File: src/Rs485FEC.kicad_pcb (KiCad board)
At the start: 2 copper layers, 24 x 27.9 mm, 19 parts, among them J1 B3B-XH-A, P1 105444-0001, Q1 DMP3099L-13, U1 FT232RL, U2 SP485E

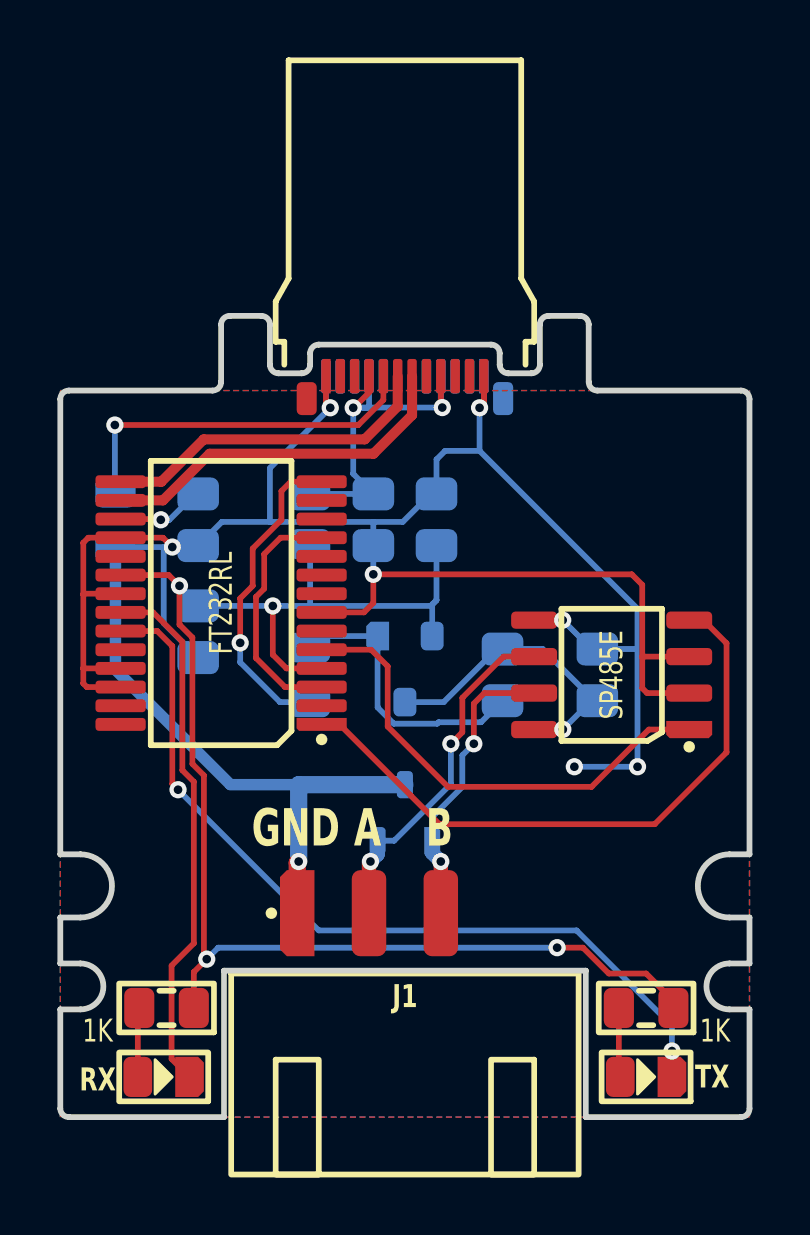
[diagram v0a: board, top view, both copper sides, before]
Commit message: Fixed TXDEN signal
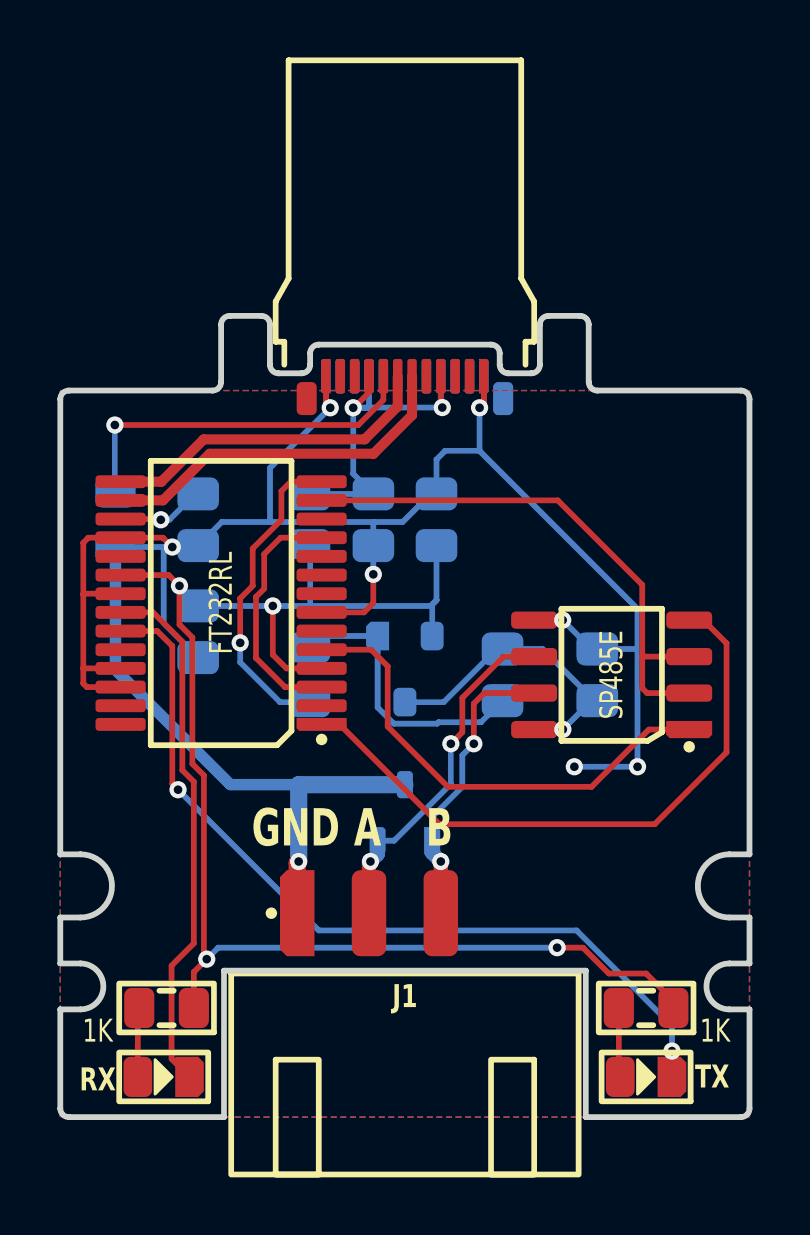
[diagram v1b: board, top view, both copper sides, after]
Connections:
- U2 pad 2: GND -> TXDEN
- U2 pad 3: GND -> TXDEN
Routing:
- net TXDEN: track 0.00 -> 19.3 mm
- net GND: track 105.1 -> 88.6 mm
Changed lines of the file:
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@@
       (net 4 "RXD") (thermal_bridge_angle 45))
     (pad "2" smd roundrect (at -2.7 -0.635 180) (size 1.6 0.6) (layers "F.Cu" "F.Paste" "F.Mask") (roundrect_rratio 0.25)
-      (net 7 "GND") (thermal_bridge_angle 45))
+      (net 19 "TXDEN") (thermal_bridge_angle 45))
     (pad "3" smd roundrect (at -2.7 0.635 180) (size 1.6 0.6) (layers "F.Cu" "F.Paste" "F.Mask") (roundrect_rratio 0.25)
-      (net 7 "GND") (thermal_bridge_angle 45))
+      (net 19 "TXDEN") (thermal_bridge_angle 45))
     (pad "4" smd roundrect (at -2.7 1.905 180) (size 1.6 0.6) (layers "F.Cu" "F.Paste" "F.Mask") (roundrect_rratio 0.25)
       (net 2 "TXD") (thermal_bridge_angle 45))
@@
   (segment (start 23.575 26.425) (end 22.1 26.425) (width 0.35) (layer "F.Cu") (net 6))
   (segment (start 29.1 30.325) (end 30.575 30.325) (width 0.2) (layer "F.Cu") (net 7))
-  (segment (start 40.265 31.865) (end 40.265 29.365) (width 0.2) (layer "F.Cu") (net 7))
-  (segment (start 39.9 29) (end 30.9 29) (width 0.2) (layer "F.Cu") (net 7))
   (segment (start 34.75 22.1) (end 34.75 23.05) (width 0.2) (layer "F.Cu") (net 7))
-  (segment (start 41.9 33.135) (end 40.435 33.135) (width 0.2) (layer "F.Cu") (net 7))
   (segment (start 23.575 27.725) (end 23.9 28.05) (width 0.2) (layer "F.Cu") (net 7))
   (segment (start 20.8 29.7) (end 20.825 29.675) (width 0.2) (layer "F.Cu") (net 7))
@@
   (segment (start 20.8 27.9) (end 20.975 27.725) (width 0.2) (layer "F.Cu") (net 7))
   (segment (start 30.575 30.325) (end 30.9 30) (width 0.2) (layer "F.Cu") (net 7))
-  (segment (start 40.265 29.365) (end 39.9 29) (width 0.2) (layer "F.Cu") (net 7))
   (segment (start 22.1 32.925) (end 20.925 32.925) (width 0.2) (layer "F.Cu") (net 7))
   (segment (start 28.25 40.8) (end 28.25 39.05) (width 0.6) (layer "F.Cu") (net 7))
@@
   (segment (start 20.975 27.725) (end 22.1 27.725) (width 0.2) (layer "F.Cu") (net 7))
   (segment (start 36.5 30.595) (end 37.495 30.595) (width 0.2) (layer "F.Cu") (net 7))
-  (segment (start 40.265 32.965) (end 40.265 31.865) (width 0.2) (layer "F.Cu") (net 7))
   (segment (start 20.825 29.675) (end 22.1 29.675) (width 0.2) (layer "F.Cu") (net 7))
-  (segment (start 41.9 31.865) (end 40.265 31.865) (width 0.2) (layer "F.Cu") (net 7))
   (segment (start 20.8 29.7) (end 20.8 27.9) (width 0.2) (layer "F.Cu") (net 7))
   (segment (start 28.25 39.05) (end 28.3 39) (width 0.6) (layer "F.Cu") (net 7))
@@
   (segment (start 34.50697 23.2) (end 34.75 22.95697) (width 0.2) (layer "F.Cu") (net 7))
   (segment (start 20.8 32.275) (end 20.8 29.7) (width 0.2) (layer "F.Cu") (net 7))
-  (segment (start 40.435 33.135) (end 40.265 32.965) (width 0.2) (layer "F.Cu") (net 7))
   (segment (start 20.8 32.8) (end 20.8 32.275) (width 0.2) (layer "F.Cu") (net 7))
   (segment (start 20.925 32.925) (end 20.8 32.8) (width 0.2) (layer "F.Cu") (net 7))
@@
   (segment (start 32.95 38.275) (end 32.95 37.45) (width 0.2) (layer "B.Cu") (net 18))
   (segment (start 34 36.4) (end 34 35.300006) (width 0.2) (layer "B.Cu") (net 18))
+  (segment (start 40.265 29.365) (end 40.265 31.865) (width 0.2) (layer "F.Cu") (net 19))
+  (segment (start 41.9 33.135) (end 40.435 33.135) (width 0.2) (layer "F.Cu") (net 19))
+  (segment (start 37.325 26.425) (end 40.265 29.365) (width 0.2) (layer "F.Cu") (net 19))
+  (segment (start 40.265 32.965) (end 40.265 31.865) (width 0.2) (layer "F.Cu") (net 19))
+  (segment (start 41.9 31.865) (end 40.265 31.865) (width 0.2) (layer "F.Cu") (net 19))
+  (segment (start 29.1 26.425) (end 37.325 26.425) (width 0.2) (layer "F.Cu") (net 19))
+  (segment (start 40.435 33.135) (end 40.265 32.965) (width 0.2) (layer "F.Cu") (net 19))
   (segment (start 27.825 32.925) (end 26.813909 31.913909) (width 0.2) (layer "F.Cu") (net 20))
   (segment (start 26.813909 29.786091) (end 27.1 29.5) (width 0.2) (layer "F.Cu") (net 20))

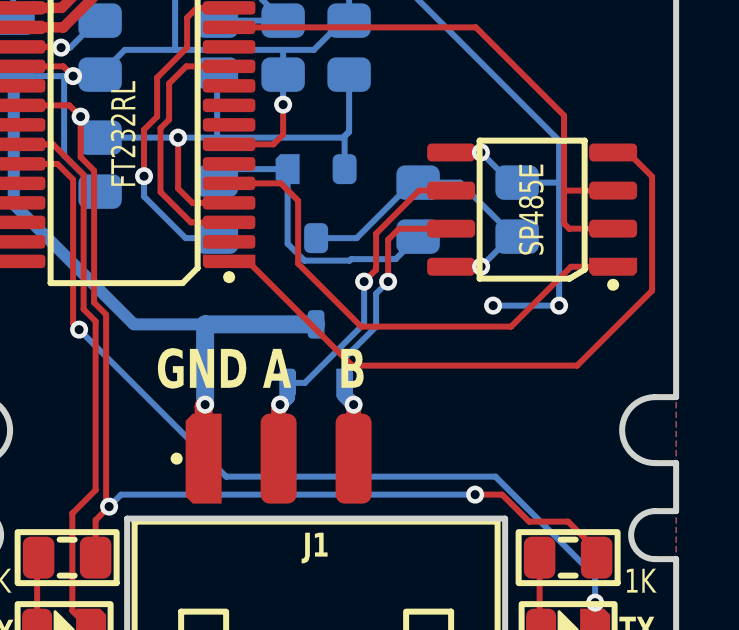
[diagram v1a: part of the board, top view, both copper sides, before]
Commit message: Added back fail-safe biased termination
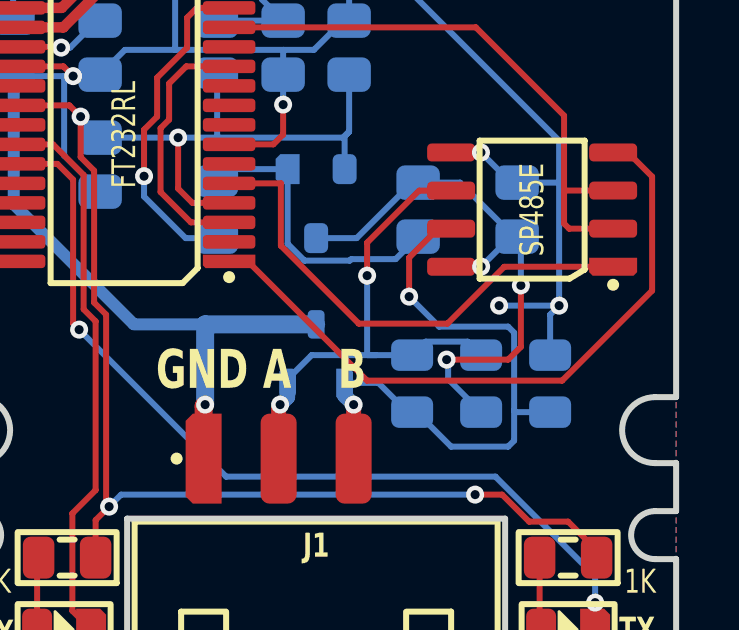
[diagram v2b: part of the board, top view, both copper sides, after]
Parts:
- added R1: 130, Medo64:R (0805), B.Cu at (35.2, 38.3)
- added R2: 750, Medo64:R (0805), B.Cu at (37.5, 38.3)
- added R3: 750, Medo64:R (0805), B.Cu at (39.8, 38.3)
- J1: value B3B-XH-A -> B4B-XH-A
- renumbered R1 to R4, R2 to R5, R3 to R6, R4 to R7
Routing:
- net B: track 10.2 -> 20.4 mm
- net 5V_SW: track 10.3 -> 18.8 mm, vias 1 -> 3
- net A: track 12.3 -> 17.4 mm
- net GND: track 88.6 -> 90.2 mm

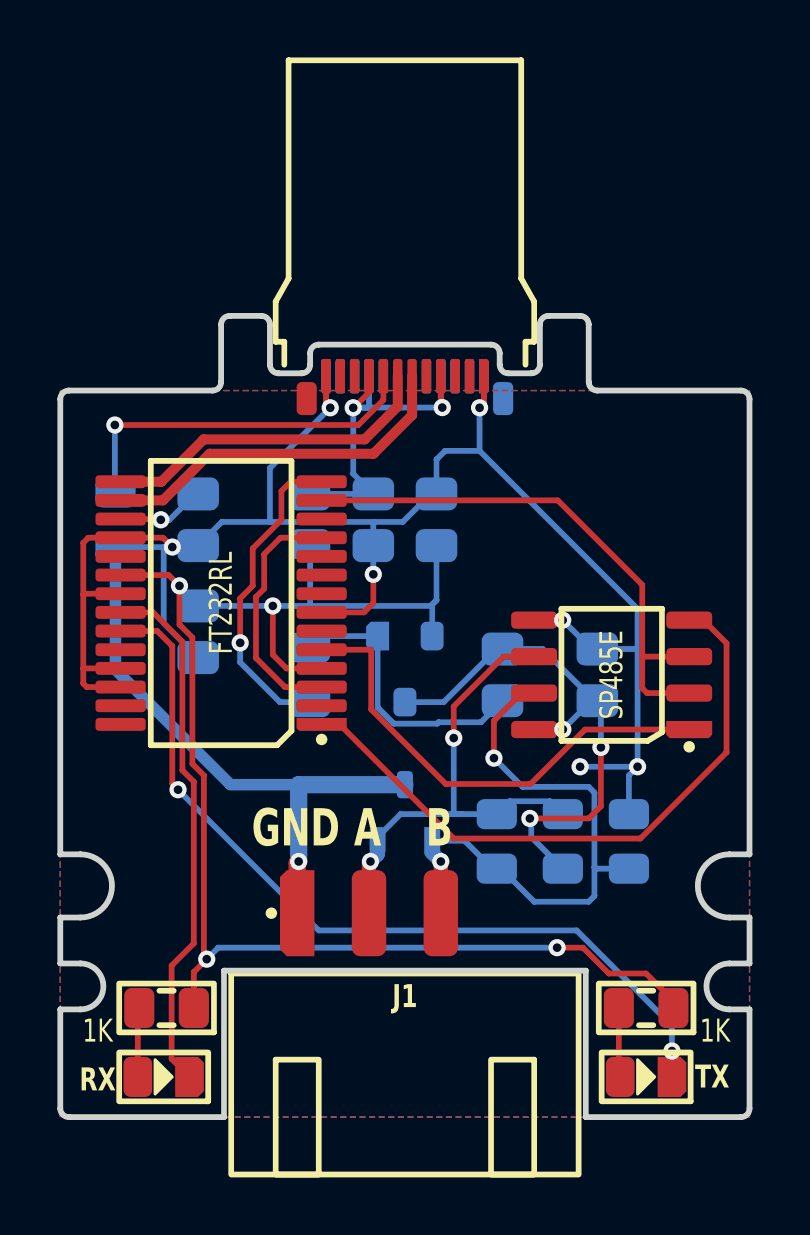
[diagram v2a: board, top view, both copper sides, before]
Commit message: Removed fail-safe termination
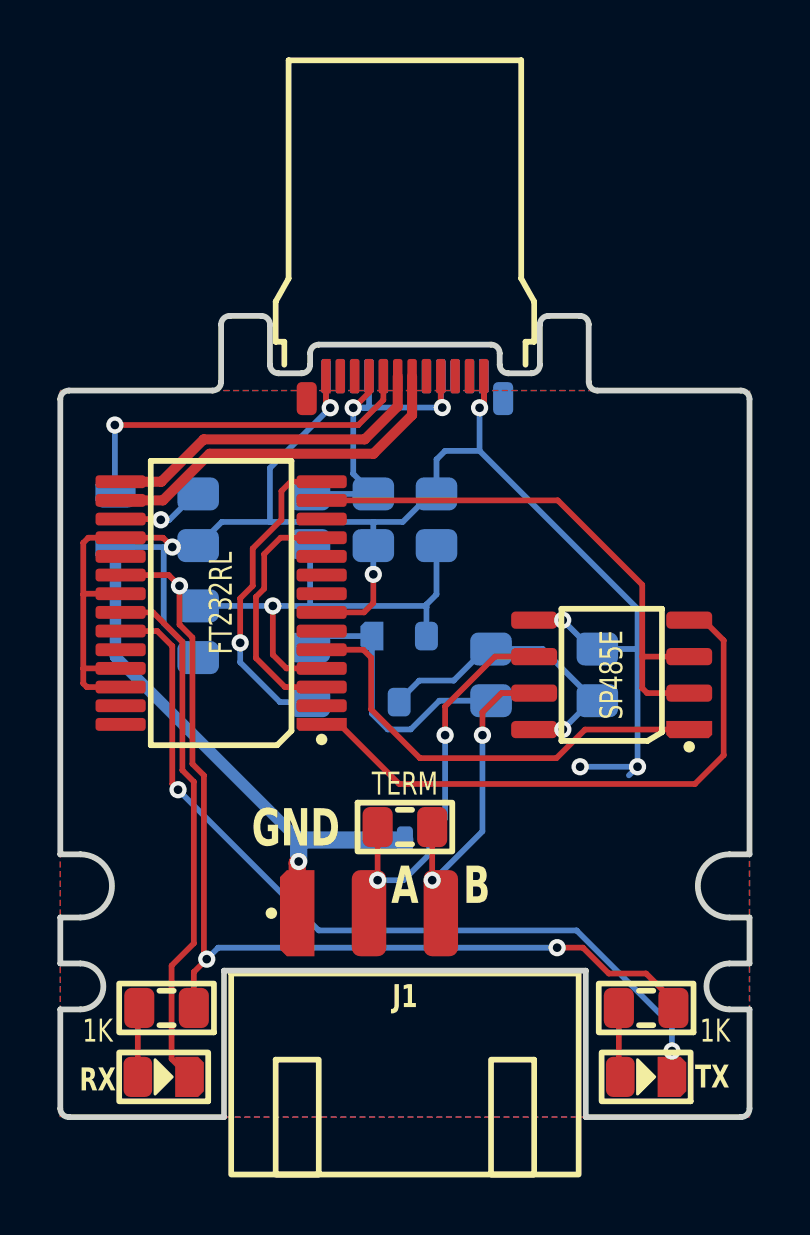
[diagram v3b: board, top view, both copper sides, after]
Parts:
- removed R2, R3: 750, Medo64:R (0805)
- R1: value 130 -> TERM; moved to F.Cu
- moved R1 3.24 mm to (32.0, 37.8), turned to 0 degrees
- moved D1 1.93 mm to (32.0, 39.2)
- moved C5 0.40 mm to (35.0, 32.5)
- moved Q1 0.20 mm to (31.8, 32.3)
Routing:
- net B: track 20.4 -> 11.1 mm
- net 5V_SW: track 18.8 -> 10.2 mm, vias 3 -> 1
- net A: track 17.4 -> 14.3 mm
- net GND: track 90.2 -> 87.5 mm
- net TXD: track 21.3 -> 19.6 mm
- net RXD: track 16.7 -> 15.8 mm

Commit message: Moving LEDs to bottom
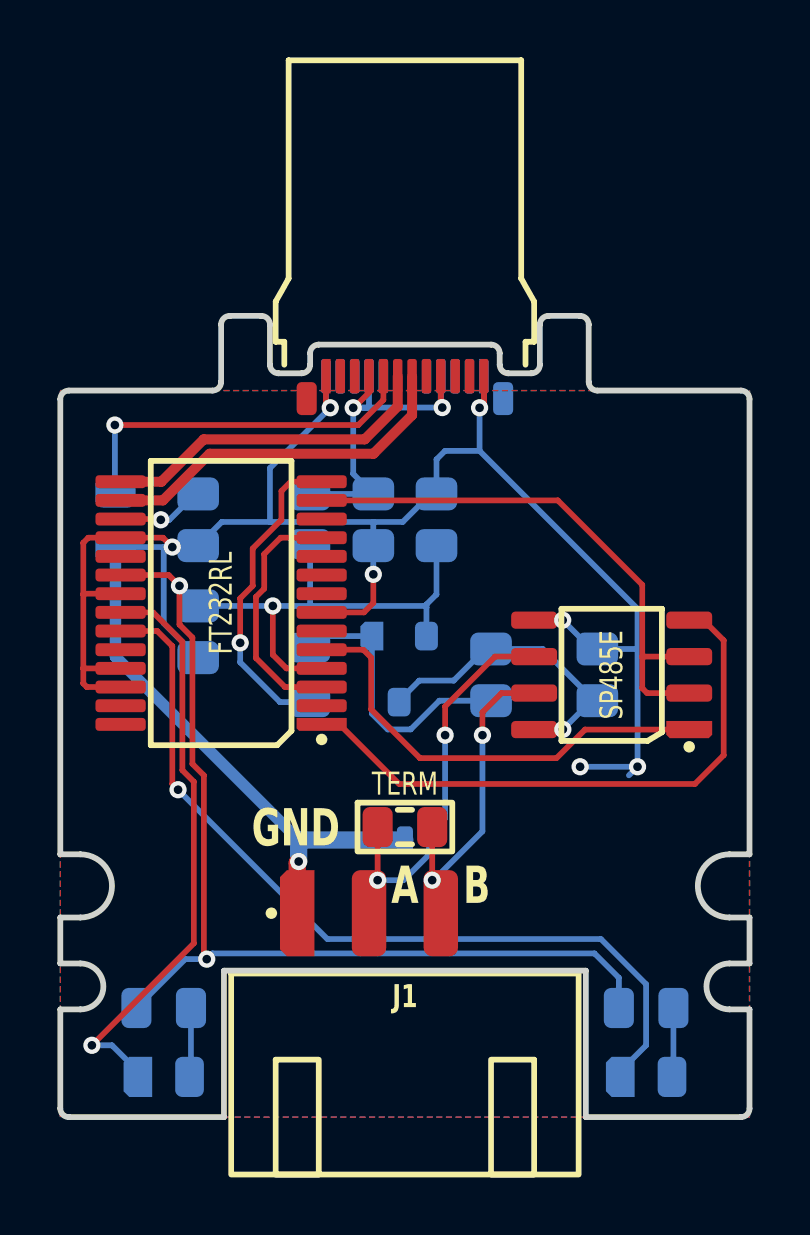
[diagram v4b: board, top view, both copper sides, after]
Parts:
- DS1, DS2, R4, R5: moved to B.Cu
- moved R4 0.10 mm to (23.6, 44.1), turned to 0 degrees
- turned DS1 to 0 degrees
- turned DS2 to 0 degrees
- turned R5 to 0 degrees
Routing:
- net LED_RXD: track 18.5 -> 20.2 mm, vias 0 -> 1
- net LED_TXD: track 29.5 -> 29.6 mm, vias 2 -> 1
- net 5V: vias 4 -> 3

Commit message: Moved termination resistor
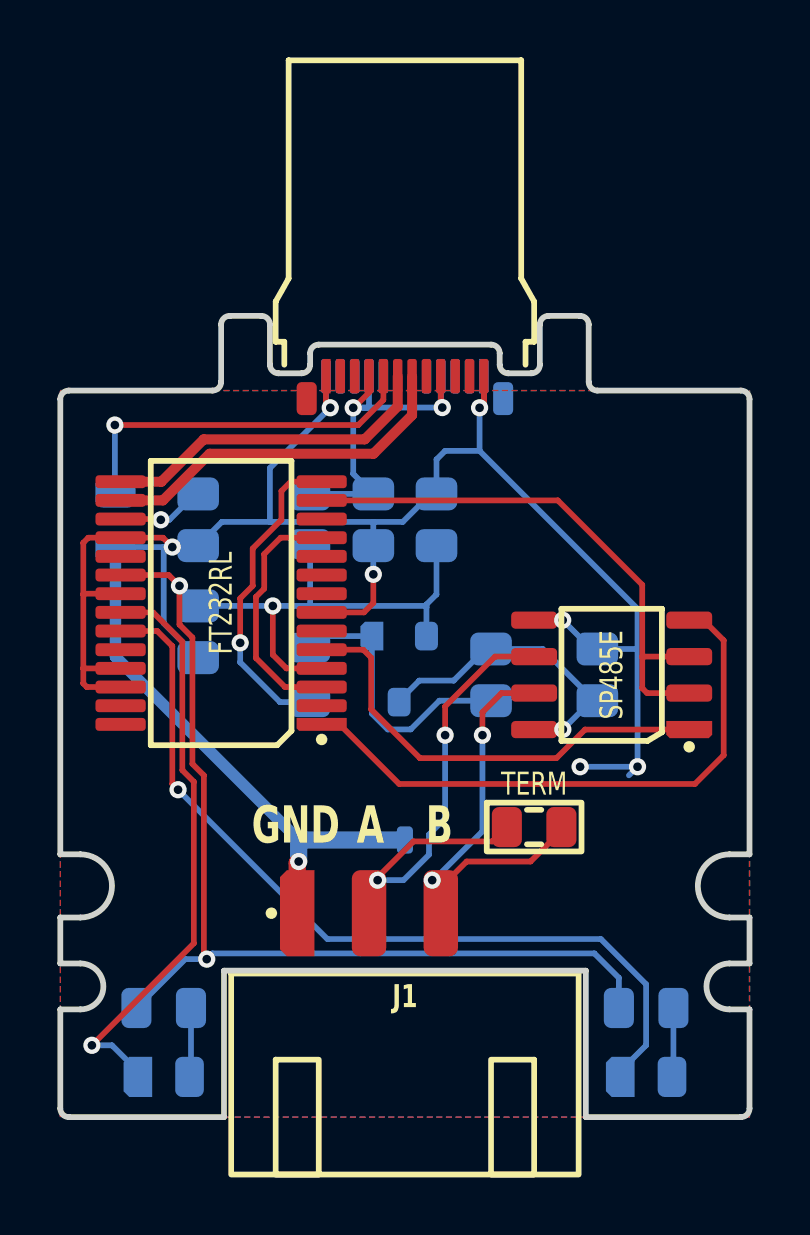
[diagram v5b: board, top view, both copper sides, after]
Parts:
- moved R1 4.50 mm to (36.5, 37.8)
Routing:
- net A: track 14.3 -> 17.1 mm
- net B: track 11.1 -> 13.9 mm
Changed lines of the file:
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@@
   (net 20 "RTS_CTS")
   (footprint "Medo64:R (0805)" (layer "F.Cu")
-    (at 32 37.8)
+    (at 36.5 37.8)
     (tags "RESC2013X70N")
     (attr smd)
@@
     (effects (font (size 0.8 0.6) (thickness 0.15) bold) (justify mirror))
   )
-  (gr_text "GND" (at 28.2 38.6) (layer "F.SilkS" knockout)
+  (gr_text "GND" (at 28.2 38.5) (layer "F.SilkS" knockout)
     (effects (font (size 1.3 0.9) (thickness 0.15) bold) (justify bottom))
   )
-  (gr_text "B" (at 34.5 40.6) (layer "F.SilkS" knockout)
+  (gr_text "B" (at 33.2 38.5) (layer "F.SilkS" knockout)
     (effects (font (size 1.3 0.9) (thickness 0.15) bold) (justify bottom))
   )
-  (gr_text "A" (at 32 40.6) (layer "F.SilkS" knockout)
+  (gr_text "A" (at 30.8 38.5) (layer "F.SilkS" knockout)
     (effects (font (size 1.3 0.9) (thickness 0.15) bold) (justify bottom))
   )
@@
   (segment (start 33.4 33.6) (end 33.4 34.6) (width 0.2) (layer "F.Cu") (net 17))
   (segment (start 35.135 31.865) (end 33.4 33.6) (width 0.2) (layer "F.Cu") (net 17))
-  (segment (start 31.05 37.8) (end 31.05 40.200025) (width 0.2) (layer "F.Cu") (net 17))
+  (segment (start 35.05 38.3) (end 35.55 37.8) (width 0.2) (layer "F.Cu") (net 17))
+  (segment (start 31.05 39.55) (end 32.3 38.3) (width 0.2) (layer "F.Cu") (net 17))
+  (segment (start 32.3 38.3) (end 35.05 38.3) (width 0.2) (layer "F.Cu") (net 17))
   (via (at 31.049975 39.65) (size 0.6) (drill 0.3) (layers "F.Cu" "B.Cu") (net 17))
   (via (at 33.4 34.6) (size 0.6) (drill 0.3) (layers "F.Cu" "B.Cu") (net 17))
@@
   (segment (start 31.95 39.65) (end 31.049975 39.65) (width 0.2) (layer "B.Cu") (net 17))
   (segment (start 36.5 33.135) (end 35.365 33.135) (width 0.2) (layer "F.Cu") (net 18))
+  (segment (start 33.500014 39.649986) (end 34.15 39) (width 0.2) (layer "F.Cu") (net 18))
   (segment (start 34.7 33.8) (end 34.7 34.6) (width 0.2) (layer "F.Cu") (net 18))
   (segment (start 35.365 33.135) (end 34.7 33.8) (width 0.2) (layer "F.Cu") (net 18))
-  (segment (start 32.95 37.8) (end 32.95 39.649986) (width 0.2) (layer "F.Cu") (net 18))
+  (segment (start 34.15 39) (end 36.375 39) (width 0.2) (layer "F.Cu") (net 18))
+  (segment (start 36.375 39) (end 37.45 37.925) (width 0.2) (layer "F.Cu") (net 18))
   (via (at 34.7 34.6) (size 0.6) (drill 0.3) (layers "F.Cu" "B.Cu") (net 18))
   (via (at 32.95 39.649986) (size 0.6) (drill 0.3) (layers "F.Cu" "B.Cu") (net 18))
